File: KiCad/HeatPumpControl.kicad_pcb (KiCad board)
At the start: 2 copper layers, 34.3 x 40.9 mm, 34 parts, among them J1 Conn_01x04_Male, J2 Conn_01x04_Male, J3 Conn_01x04_Male, Q1 2N2222A, U1 TSOP23xx, U2 SeedStudio XIAO ESP32 C3 v1

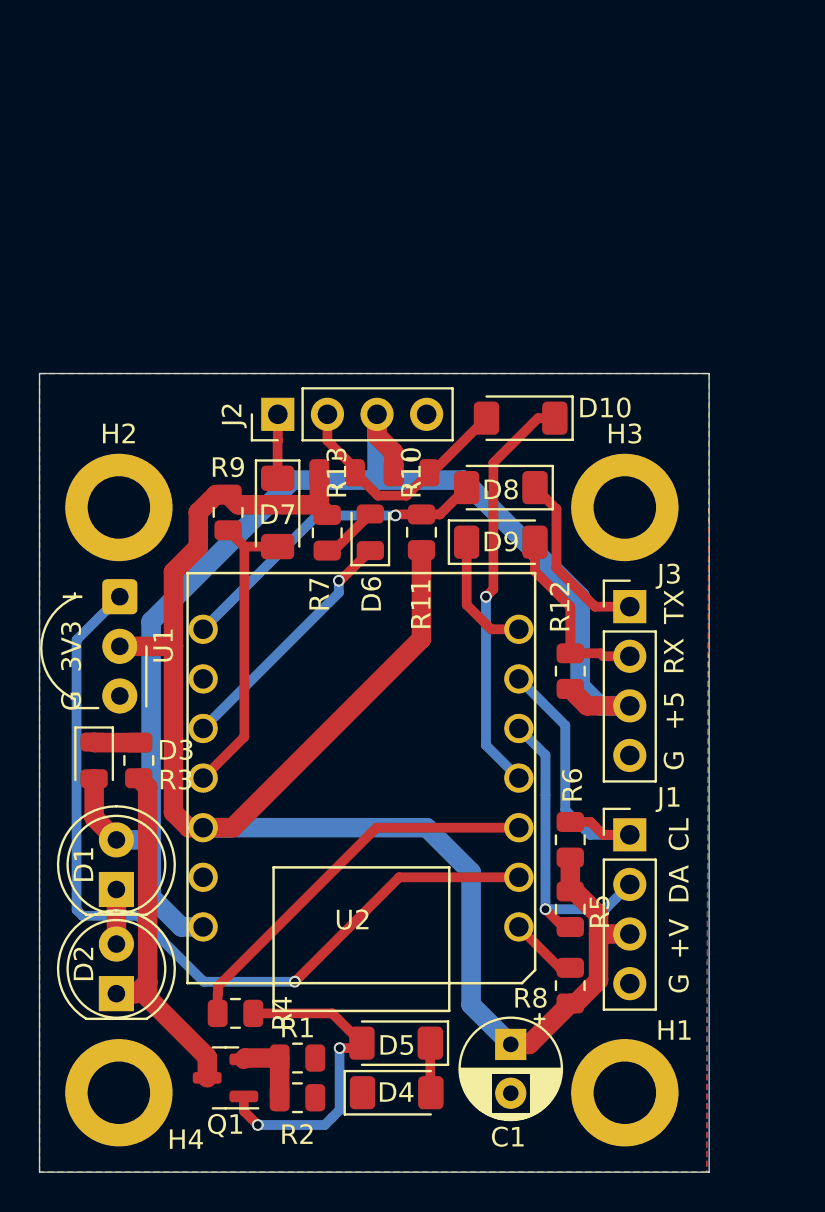
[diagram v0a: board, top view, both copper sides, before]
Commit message: ESP32C6 support
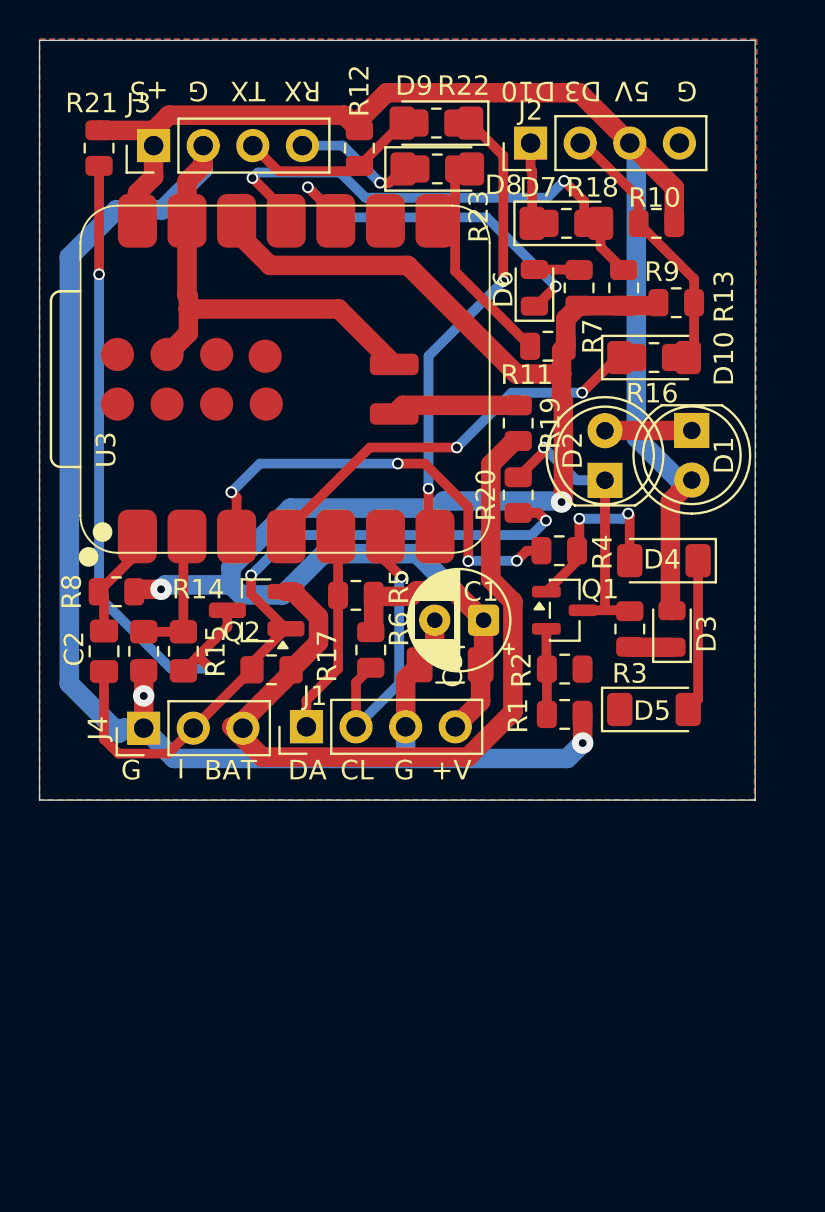
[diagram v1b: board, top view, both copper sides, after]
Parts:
- removed H1, H2, H3, H4: MountingHole_Pad, MountingHole:MountingHole_3.2mm_M3_ISO14580_Pad
- removed U1: TSOP23xx, OptoDevice:Vishay_MOLD-3Pin
- removed U2: SeedStudio XIAO ESP32 C3 v1, LOCAL1:XIAO_ESP32C3_THT
- added C2: 100nF, Capacitor_SMD:C_0805_2012Metric_Pad1.18x1.45mm_HandSolder, F.Cu at (139.2, 116.2)
- added C3: 10uF, Capacitor_SMD:C_1206_3216Metric_Pad1.33x1.80mm_HandSolder, F.Cu at (156.9, 116.9)
- added J4: Conn_01x03_Male, Connector_PinHeader_2.54mm:PinHeader_1x03_P2.54mm_Vertical, F.Cu at (141.2, 120.1)
- added Q2: Q_PMOS_GDS, Package_TO_SOT_SMD:SOT-23_Handsoldering, F.Cu at (147.0, 114.1)
- added R14: 20k, Resistor_SMD:R_0805_2012Metric_Pad1.20x1.40mm_HandSolder, F.Cu at (141.2, 116.2)
- added R15: 51.2k, Resistor_SMD:R_0805_2012Metric_Pad1.20x1.40mm_HandSolder, F.Cu at (143.3, 116.2)
- added R16: 0, Resistor_SMD:R_0805_2012Metric, F.Cu at (167.4, 101.2)
- added R17: 82k, Resistor_SMD:R_0805_2012Metric_Pad1.20x1.40mm_HandSolder, F.Cu at (147.8, 117.2)
- added R18: 0, Resistor_SMD:R_0805_2012Metric, F.Cu at (162.9, 94.3)
- added R19: 0, Resistor_SMD:R_0805_2012Metric, F.Cu at (160.4, 104.5)
- added R20: 0, Resistor_SMD:R_0805_2012Metric, F.Cu at (160.4, 108.2)
- added R21: 0, Resistor_SMD:R_0805_2012Metric, F.Cu at (138.9, 90.4)
- added R22: 0, Resistor_SMD:R_0805_2012Metric, F.Cu at (156.2, 89.2)
- added R23: 0, Resistor_SMD:R_0805_2012Metric, F.Cu at (156.3, 91.5)
- added U3: XIAO-ESP32-C6-SMD, LOCAL1:XIAO-ESP32-C6-SMD, F.Cu at (148.5, 102.0)
- moved D1 37.7 mm to (169.3, 104.9), turned to -90 degrees
- moved D2 36.3 mm to (164.8, 107.4)
- moved J3 33.9 mm to (141.7, 90.3), turned to 90 degrees
- moved R8 30.8 mm to (139.8, 113.2), turned to 180 degrees
- moved D3 30.3 mm to (168.3, 115.1), turned to 90 degrees
- moved Q1 29.6 mm to (162.8, 114.1), turned to 0 degrees
- moved R4 28.9 mm to (162.5, 111.1)
- moved R12 28.9 mm to (152.3, 90.4), turned to -90 degrees
- moved D4 28.3 mm to (167.9, 111.6)
- moved R3 26.0 mm to (166.1, 115.1), turned to -90 degrees
- moved R2 25.9 mm to (162.8, 117.1)
- moved D5 23.6 mm to (167.4, 119.2)
- moved R9 23.3 mm to (165.8, 97.6), turned to 90 degrees
- moved R1 22.3 mm to (162.8, 119.4)
- moved C1 21.8 mm to (158.6, 114.6), turned to 180 degrees
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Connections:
- net /GPIO10 renamed /D10
- net /LED1 renamed Net-(Q1-E)
- net /LED2 renamed //ON
- D10 pad 1: /GPIO5 -> /D3
- D6 pad 1: /GPIO9 -> /D9
- J1 pad 1: /SCL -> /SDA
- J1 pad 2: /SDA -> /SCL
- J1 pad 3: +3V3 -> GND
- J1 pad 4: GND -> +3V3
- J3 pad 1: Net-(D8-K) -> +5V
- J3 pad 2: Net-(D9-A) -> GND
- J3 pad 3: +5V -> Net-(D9-A)
- J3 pad 4: GND -> Net-(D8-K)
- R4 pad 1: /GPIO4 -> /D2
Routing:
- net GND: track 0.00 -> 95.5 mm, vias 0 -> 2
- net /GPIO3: track 43.3 -> 0.00 mm, vias 1 -> 0
- net +VBAT: track 0.00 -> 40.9 mm
- net Net-(J4-Pin_2): track 0.00 -> 37.3 mm, vias 0 -> 2
- net Net-(Q2-D): track 0.00 -> 34.3 mm, vias 0 -> 2
- net /D2: track 0.00 -> 22.8 mm, vias 0 -> 4
- net /D3: track 0.00 -> 21.9 mm, vias 0 -> 2
- net /GPIO5: track 21.1 -> 0.00 mm, vias 1 -> 0
- net /GPIO4: track 20.2 -> 0.00 mm
- net /D9: track 0.00 -> 18.6 mm, vias 0 -> 2
- net /TX: track 6.40 -> 24.4 mm, vias 0 -> 2
- net /GPIO9: track 12.7 -> 0.00 mm, vias 1 -> 0
- net /D10: track 15.6 -> 26.2 mm, vias 0 -> 2
- net Net-(D4-A): track 16.9 -> 9.49 mm
- net Net-(U3-GPIO1_A1_D1): track 0.00 -> 6.99 mm
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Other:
- board size 34.3 x 40.9 mm -> 36.6 x 38.9 mm
- board text added: "BAT"
- board text added: "D10"
- board text added: "D3"
- board text added: "Heat pump controller rev 4.0 (C) 2025 - Hans Rune Bue <email@hansrune.net>"
- board text removed: "3V3"
- board text removed: "Heat pump controller rev 2.0.1 (C) 2023 - Hans Rune Bue <email@hansrune.net>"
- board text removed: "O"

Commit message: Diode foorptint changes
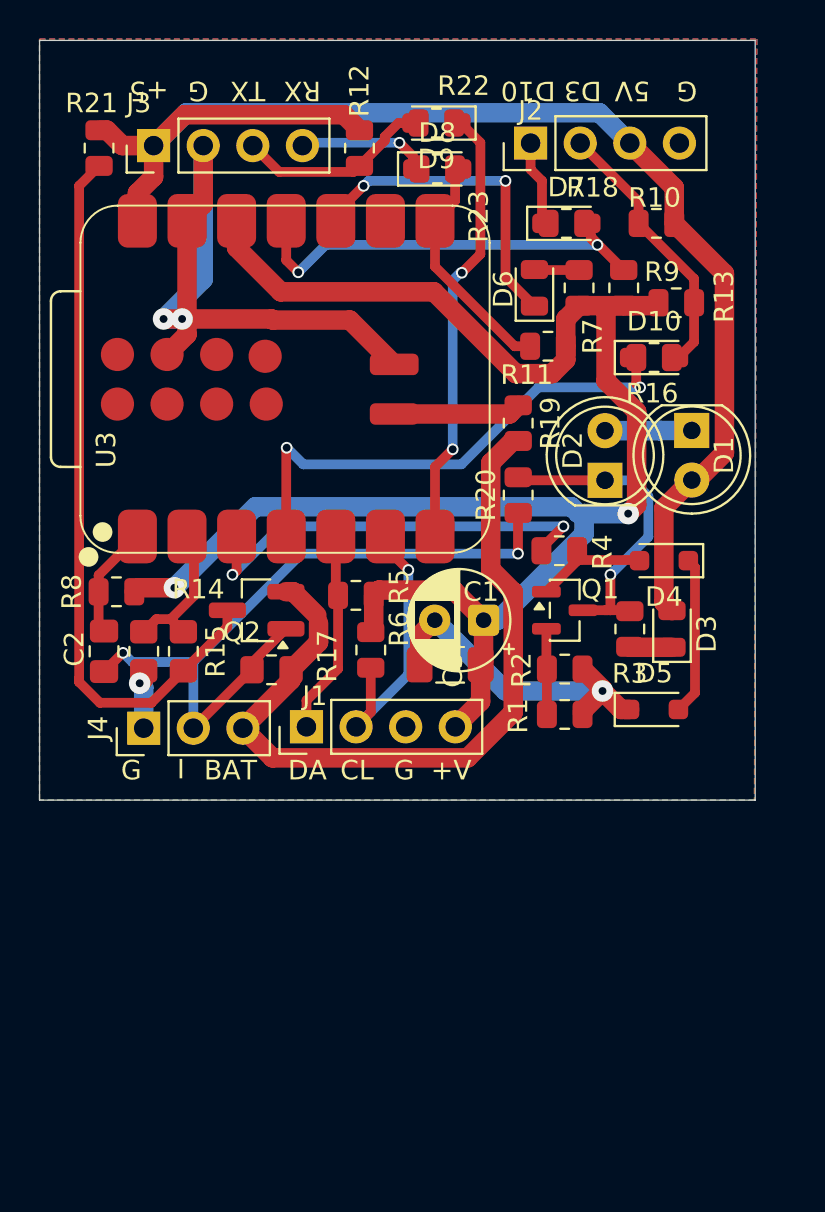
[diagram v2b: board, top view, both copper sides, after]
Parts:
- D10, D4, D5, D7, D8, D9: footprint Diode_SMD:D_MiniMELF -> Diode_SMD:D_SOD-323_HandSoldering
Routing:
- net GND: track 95.5 -> 55.9 mm, vias 2 -> 4
- net +5V: track 66.0 -> 72.1 mm
- net /D3: track 21.9 -> 26.6 mm
- net /D10: track 26.2 -> 22.4 mm
- net Net-(D4-A): track 9.49 -> 5.96 mm, vias 2 -> 0
- net Net-(Q2-D): track 34.3 -> 37.5 mm, vias 2 -> 0
- net /D9: track 18.6 -> 16.8 mm
- net /TX: track 24.4 -> 22.9 mm
- net //ON: track 15.0 -> 16.1 mm
- net /D2: track 22.8 -> 21.7 mm, vias 4 -> 2
- net +VBAT: track 40.9 -> 40.1 mm
- net Net-(J4-Pin_2): track 37.3 -> 36.6 mm

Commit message: Add 5-3.3 V divider for Rx
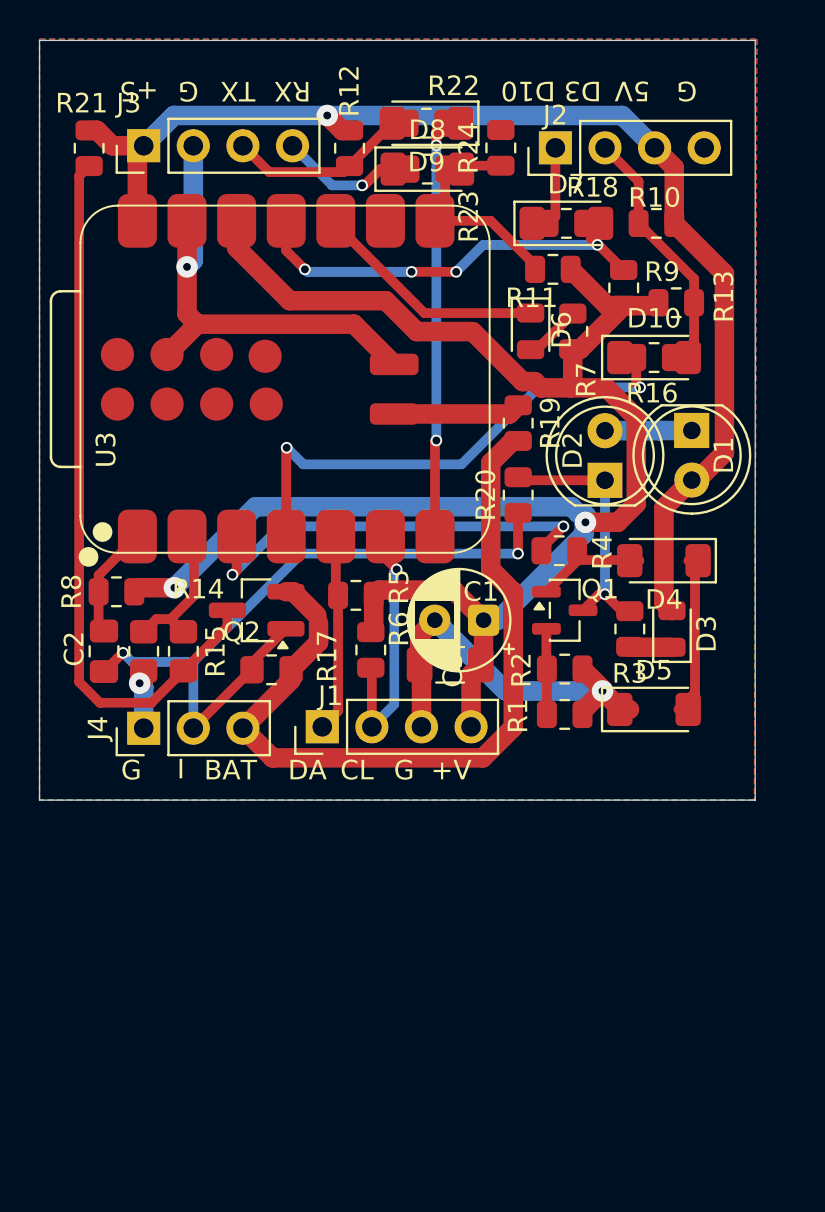
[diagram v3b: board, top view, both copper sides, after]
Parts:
- added R24: 3k3, Resistor_SMD:R_0805_2012Metric, F.Cu at (159.5, 90.4)
- D10, D4, D5, D7, D8, D9: footprint Diode_SMD:D_SOD-323_HandSoldering -> Diode_SMD:D_MiniMELF
- R23: value 0 -> 18k
- moved R11 3.95 mm to (162.2, 96.6)
- moved R7 2.25 mm to (163.2, 99.8)
- moved D6 2.24 mm to (161.0, 99.8), turned to -90 degrees
- moved J2 1.29 mm to (162.3, 90.4)
- moved J1 0.81 mm to (150.4, 120.1)
- moved D8 0.51 mm to (155.7, 91.5)
- moved D9 0.51 mm to (155.7, 89.2)
- moved J3 0.51 mm to (141.2, 90.3)
- moved R12 0.51 mm to (151.8, 90.4)
- moved R22 0.51 mm to (155.7, 89.2)
- moved R23 0.51 mm to (155.7, 91.5)
- moved R21 0.51 mm to (138.4, 90.4)
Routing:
- net +5V: track 72.1 -> 62.8 mm, vias 0 -> 1
- net GND: track 55.9 -> 48.9 mm, vias 4 -> 3
- net /D9: track 16.8 -> 12.0 mm, vias 2 -> 0
- net //ON: track 16.1 -> 13.4 mm
- net /RX: track 12.3 -> 10.3 mm
- net +3V3: track 89.5 -> 91.3 mm
- net /TX: track 22.9 -> 21.4 mm
- net /SCL: track 14.7 -> 13.6 mm
- net Net-(D9-A): track 10.2 -> 9.25 mm
- net Net-(D10-A): track 14.1 -> 13.3 mm
- net Net-(D7-K): track 4.69 -> 4.01 mm
- net Net-(D8-K): track 6.99 -> 6.34 mm
- net Net-(D6-A): track 2.30 -> 2.93 mm
- net /D10: track 22.4 -> 22.1 mm, vias 2 -> 4

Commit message: Added combined C3/C6 module footprint
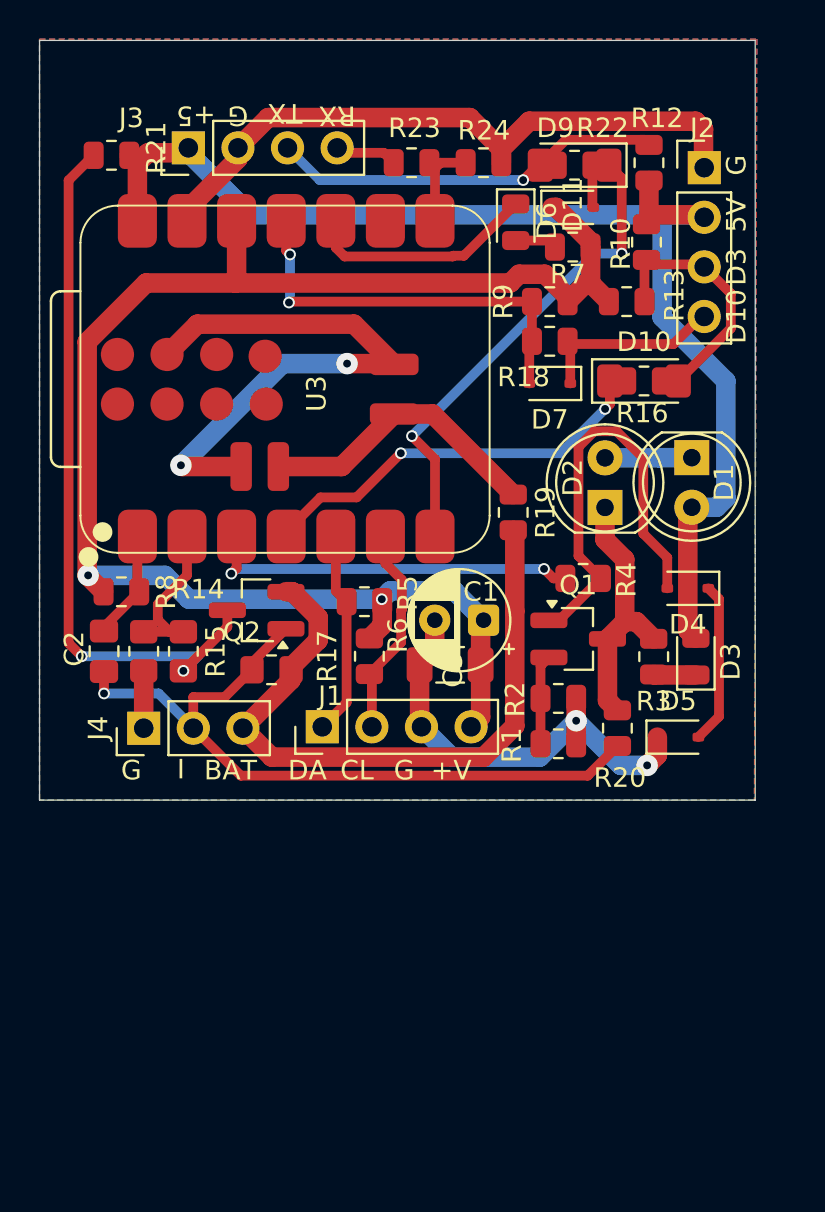
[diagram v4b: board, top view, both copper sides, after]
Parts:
- removed D8: 1N4148, Diode_SMD:D_MiniMELF
- removed R11: 4k7, Resistor_SMD:R_0805_2012Metric
- added D11: 1N4148, Diode_SMD:D_SOD-323, F.Cu at (163.2, 93.5)
- D4, D5, D7: footprint Diode_SMD:D_MiniMELF -> Diode_SMD:D_SOD-323
- Q1: footprint Package_TO_SOT_SMD:SOT-23 -> Package_TO_SOT_SMD:SOT-23_Handsoldering
- R23: value 18k -> 2.2k
- R24: value 3k3 -> 4.3k
- U3: footprint LOCAL1:XIAO-ESP32-C6-SMD -> LOCAL1:XIAO-ESP32-C3C6-SMD
- moved R12 15.4 mm to (167.1, 91.2), turned to 90 degrees
- moved R20 13.0 mm to (165.5, 120.1)
- moved D7 8.24 mm to (162.0, 102.5), turned to 180 degrees
- moved D9 7.88 mm to (163.3, 91.3)
- moved R22 7.88 mm to (163.3, 91.3)
- moved J2 7.69 mm to (169.9, 91.4), turned to 0 degrees
- moved R18 6.10 mm to (162.0, 100.3), turned to 180 degrees
- moved D6 5.64 mm to (160.3, 94.2)
- moved R19 4.58 mm to (160.1, 109.1)
- moved R7 4.32 mm to (163.2, 95.5), turned to 180 degrees
- moved R9 3.85 mm to (162.0, 98.3), turned to 180 degrees
- moved R13 2.54 mm to (166.0, 98.3)
- moved J3 2.29 mm to (143.5, 90.4)
- moved D5 1.87 mm to (168.6, 120.6)
- moved D3 1.87 mm to (169.5, 116.5)
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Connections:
- net //ON renamed /ON
- J2 pad 1: Net-(D7-K) -> GND
- J2 pad 2: Net-(D10-A) -> +5V
- J2 pad 3: +5V -> Net-(D10-A)
- J2 pad 4: GND -> Net-(D7-K)
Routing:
- net GND: track 48.9 -> 89.3 mm, vias 3 -> 4
- net Net-(D4-A): track 5.96 -> 22.2 mm
- net Net-(D9-A): track 9.25 -> 21.0 mm, vias 0 -> 1
- net +3V3: track 91.3 -> 80.3 mm
- net /BAT: track 6.53 -> 14.9 mm
- net /TX: track 21.4 -> 28.1 mm
- net +VBAT: track 40.5 -> 34.7 mm
- net Net-(D7-K): track 4.01 -> 9.68 mm
- net /RX: track 10.3 -> 4.78 mm
- net /D3: track 26.6 -> 21.5 mm
- net Net-(J3-Pin_4): track 6.34 -> 3.11 mm, vias 1 -> 0
- net /SCL: track 13.6 -> 10.8 mm, vias 1 -> 0
- net /D2: track 21.7 -> 19.4 mm
- net Net-(J4-Pin_2): track 36.6 -> 37.8 mm, vias 2 -> 1
- net /D10: track 22.1 -> 21.0 mm, vias 4 -> 2
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
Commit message: Manufacturing for v4.0
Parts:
- D1, D2: moved to B.Cu
- moved D3 13.3 mm to (165.7, 103.8)
- moved R3 9.08 mm to (165.7, 107.6), turned to 90 degrees
- moved R1 8.73 mm to (170.4, 117.2)
- moved R2 8.62 mm to (170.4, 115.2)
- moved D4 8.20 mm to (166.5, 120.8)
- moved R20 7.27 mm to (165.0, 112.9), turned to 0 degrees
- moved D2 6.13 mm to (170.1, 112.0)
- moved D10 3.71 mm to (163.8, 100.3)
- moved R16 3.71 mm to (163.8, 100.3)
- moved R4 3.34 mm to (163.6, 115.8), turned to -90 degrees
- moved Q1 3.32 mm to (166.5, 116.8), turned to 90 degrees
- moved D7 2.54 mm to (162.9, 104.9)
- moved R18 2.54 mm to (162.9, 102.7)
- moved R19 2.44 mm to (162.2, 107.8)
- moved D5 2.06 mm to (170.2, 119.4), turned to 180 degrees
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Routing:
- net Net-(D4-A): track 22.2 -> 5.13 mm
- net +5V: track 63.9 -> 53.6 mm
- net Net-(D4-K): track 8.28 -> 2.20 mm
- net /D10: track 21.0 -> 26.3 mm
- net /D2: track 19.4 -> 24.7 mm
- net Net-(D10-A): track 13.6 -> 8.38 mm
- net /TX: track 28.1 -> 24.8 mm
- net Net-(J4-Pin_2): track 37.8 -> 35.2 mm, vias 1 -> 3
- net GND: track 89.3 -> 91.3 mm, vias 4 -> 3
- net +VBAT: track 34.7 -> 36.6 mm
- net +3V3: track 80.3 -> 81.9 mm
- net /ON: track 13.2 -> 11.8 mm
- net /D3: track 21.5 -> 20.3 mm
- net Net-(D7-K): track 9.68 -> 10.8 mm
- net /BAT: track 14.9 -> 15.7 mm
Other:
- board size 36.6 x 38.9 mm -> 38.2 x 37.4 mm

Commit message: Add GPIO descriptions and other texts
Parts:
- added D8: 1N4148, Diode_SMD:D_SOD-323, F.Cu at (165.0, 112.9)
- R15: value 51.2k -> 68k
- R17: value 82k -> 1M

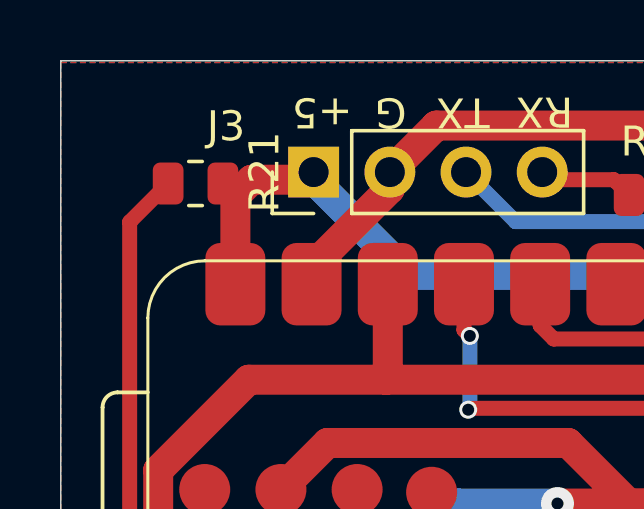
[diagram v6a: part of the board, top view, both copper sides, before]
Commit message: Add diode for VBAT -> 5V
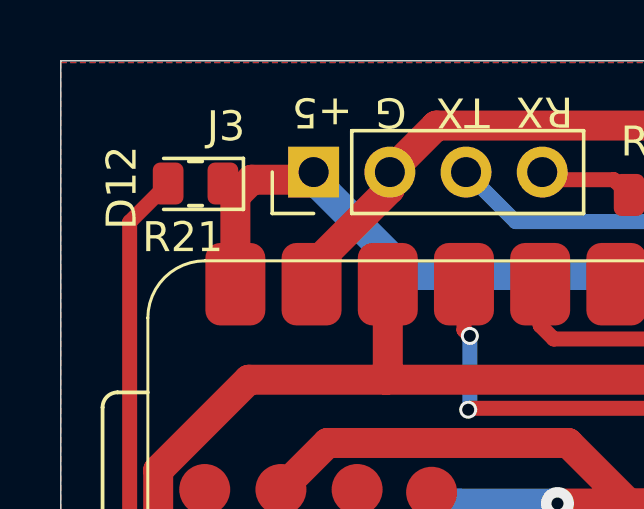
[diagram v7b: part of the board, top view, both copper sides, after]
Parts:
- added D12: 1N4007, Diode_SMD:D_SOD-323, F.Cu at (140.4, 90.6)
